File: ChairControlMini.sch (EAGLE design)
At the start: 36 parts, among them J1 Digital_0_7, J2 Analog, J3 Digital_8_13, J4 Analog, J5 Digital_0_7, SW1 SWITCH-DPDT3, X1 INPUT, X2 OUTPUT, X4 INPUT

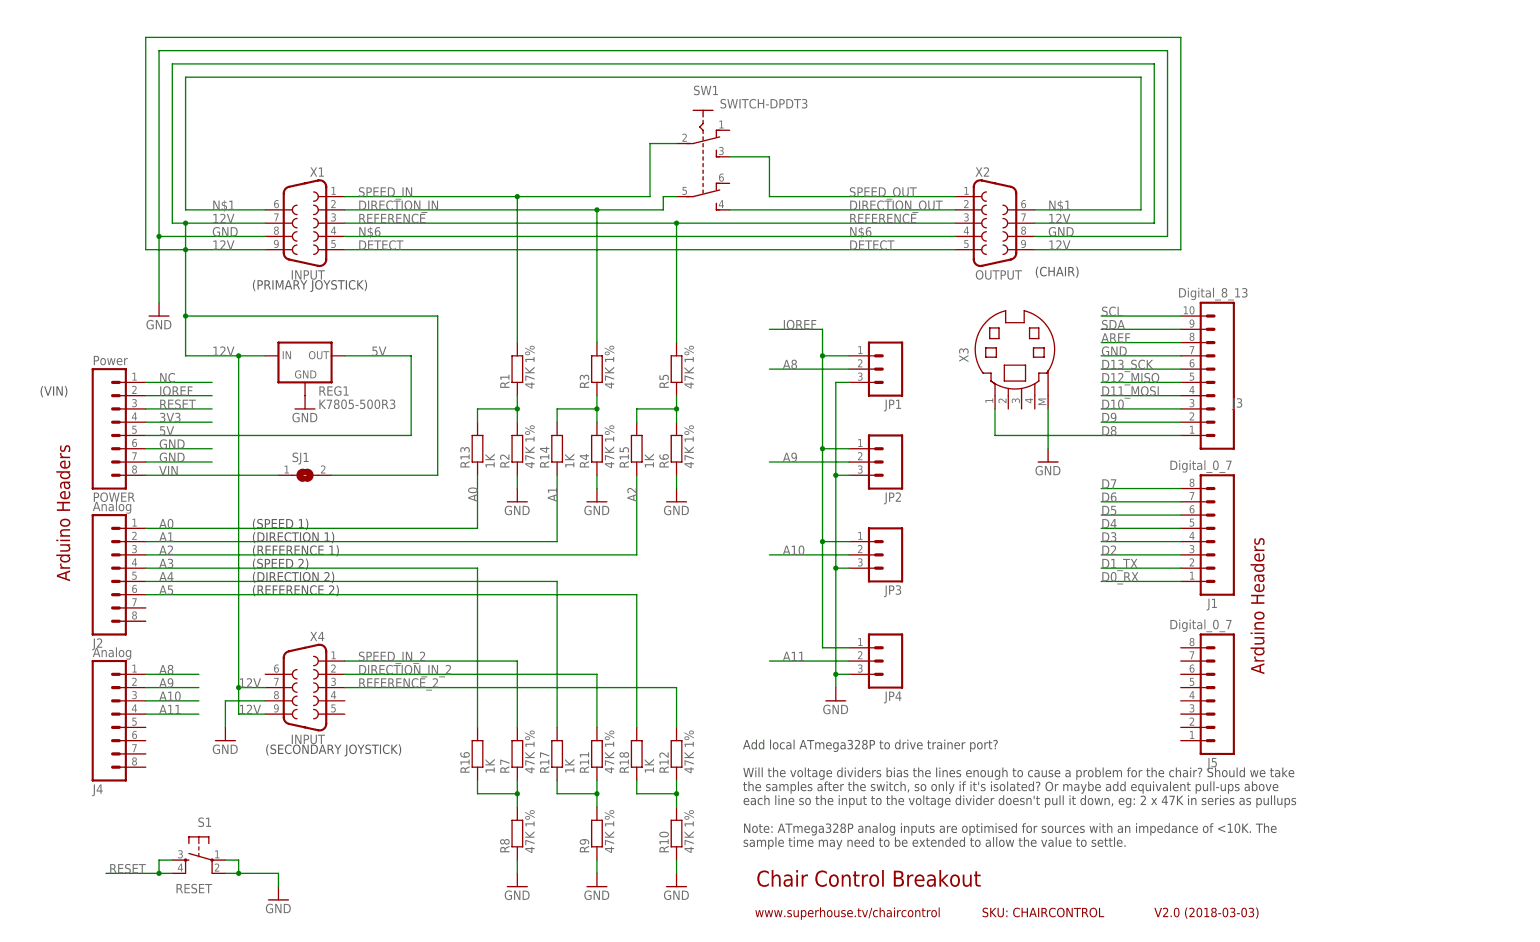
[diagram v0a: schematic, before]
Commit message: Added CAN interface and removed second joystick input
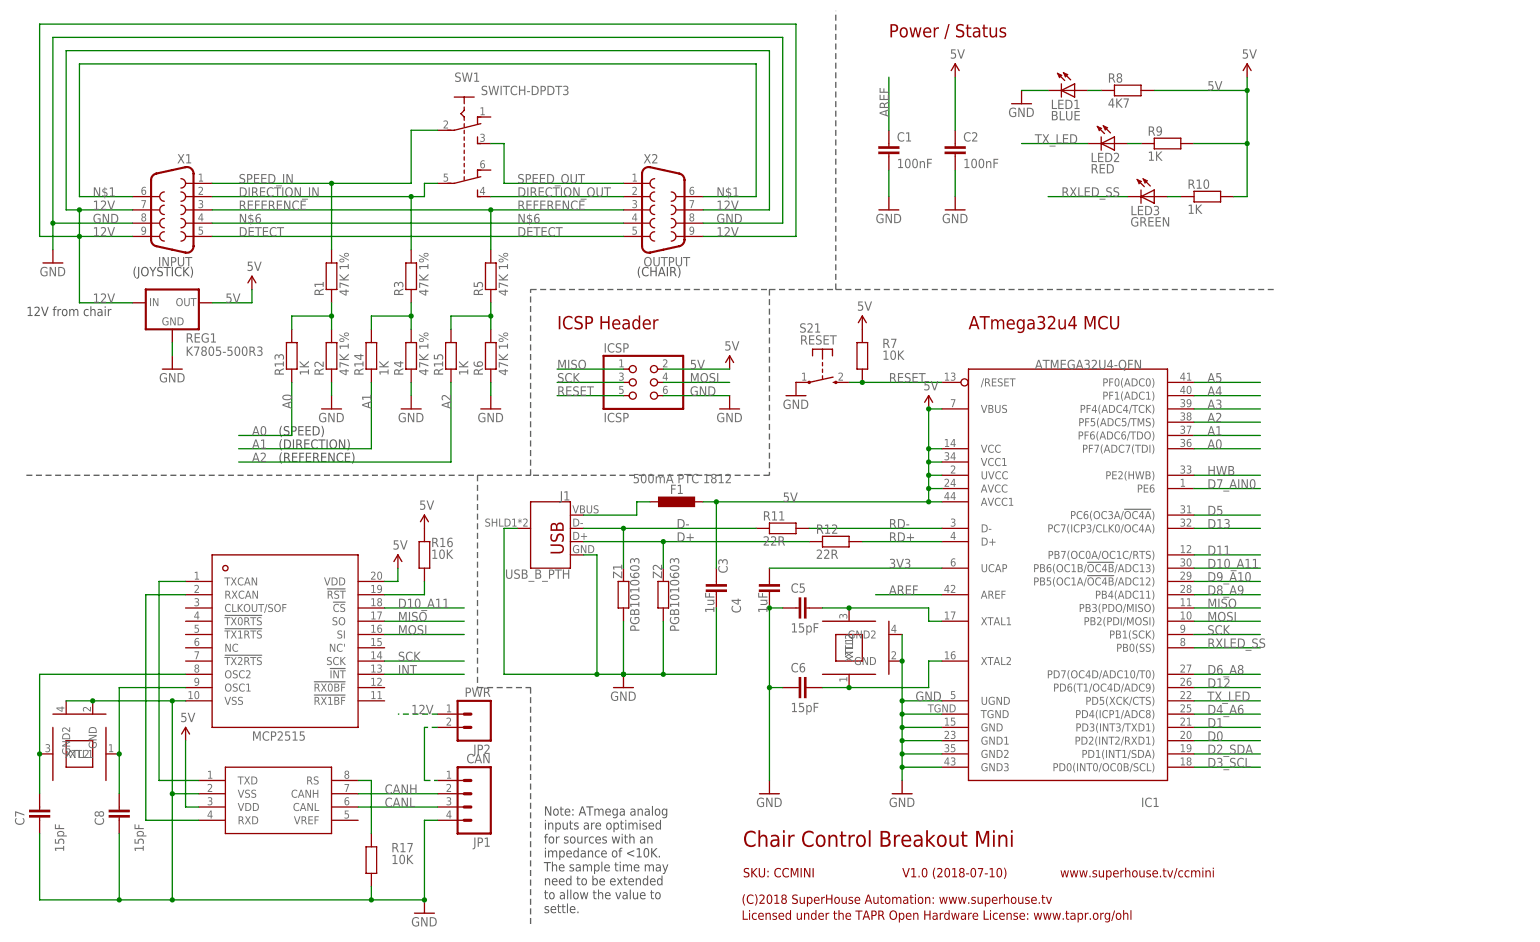
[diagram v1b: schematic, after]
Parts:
- removed J2, J4: Analog, freetronics-jon:M08PTH
- removed J3: Digital_8_13, freetronics-original:M100.1
- removed J5: Digital_0_7, freetronics:M08
- removed JP3, JP4: (no value), freetronics-jon:M03PTH
- removed POWER: Power, freetronics-original:M08
- removed R18: 1K, freetronics-jon:RESISTOR0603
- removed S1: RESET, freetronics:TAC_SWITCHPTH
- removed SJ1: (no value), freetronics-jon:SJN
- removed X3: (no value), freetronics-jon:MD04S
- removed X4: INPUT, SparkFun-Connectors:DB9MALE
- added C1, C2: 100nF, freetronics-master-v1.1:CAP0603
- added C3, C4: 1uF, freetronics-master-v1.1:CAP0603
- added C5, C6, C7, C8: 15pF, freetronics-master-v1.1:CAP0603
- added F1: 500mA PTC 1812, rcl:L-EUL1812
- added IC1: ATMEGA32U4-QFN, freetronics-jon:ATMEGA32U4-QFN
- added ICSP: ICSP, pinhead:PINHD-2X3
- added LED1: BLUE, freetronics-jon:LED0603
- added LED2: RED, freetronics-jon:LED0603
- added LED3: GREEN, freetronics-jon:LED0603
- added S21: RESET, freetronics-jon:TAC_SWITCH_2PINSMT
- added U$4: MCP2515, MCP2515:MCP2515
- added U1: MCP2551, freetronics-original:MCP2551
- added XTL1, XTL2: 16MHz, freetronics-jon:CRYSTAL-GND3X2
- added Z1, Z2: PGB1010603, freetronics-master-v1.1:RESISTOR0603
- J1: value Digital_0_7 -> USB_B_PTH; device freetronics:M08 -> SparkFun-Connectors:USB_B_PTH
- JP1: value (none) -> CAN; device freetronics-jon:M03PTH -> freetronics-jon:M04PTH
- JP2: value (none) -> PWR; device freetronics-jon:M03PTH -> freetronics-jon:M02PTH
- R10, R9: value 47K 1% -> 1K
- R11, R12: value 47K 1% -> 22R
- R16, R17: value 1K -> 10K; device freetronics-jon:RESISTOR0603 -> freetronics-master-v1.1:RESISTOR0603
- R7: value 47K 1% -> 10K; device freetronics-jon:RESISTOR0603 -> freetronics-master-v1.1:RESISTOR0603
- R8: value 47K 1% -> 4K7
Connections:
- removed net A10: J4.3, JP3.2
- removed net A11: J4.4, JP4.2
- removed net A8: J4.1, JP1.2
- removed net A9: J4.2, JP2.2
- removed net D0_RX: J1.1
- removed net D10: J3.3
- removed net D11_MOSI: J3.4
- removed net D12_MISO: J3.5
- removed net D13_SCK: J3.6
- removed net D1_TX: J1.2
- removed net D2: J1.3
- removed net D3: J1.4
- removed net D4: J1.5
- removed net D6: J1.7
- removed net D7: J1.8
- removed net D8: J3.1, X3.1
- removed net D9: J3.2
- removed net DIRECTION_IN_2: R11.2, X4.2
- removed net IOREF: JP1.1, JP2.1, JP3.1, JP4.1, POWER.2
- removed net NC: POWER.1
- removed net REFERENCE_2: R12.2, X4.3
- removed net SCL: J3.10
- removed net SDA: J3.9
- removed net SPEED_IN_2: R7.2, X4.1
- removed net VIN: POWER.8, SJ1.1
- new net CANH: JP1.2, U1.CANH
- new net CANL: JP1.3, U1.CANL
- new net D+: J1.D+, R12.1, Z2.2
- new net D-: J1.D-, R11.1, Z1.2
- new net D0: IC1.PD2(INT2/RXD1)
- new net D1: IC1.PD3(INT3/TXD1)
- new net D10_A11: IC1.PB6(OC1B/!OC4B!/ADC13), U$4.!CS
- new net D11: IC1.PB7(OC0A/OC1C/RTS)
- new net D12: IC1.PD6(T1/OC4D/ADC9)
- new net D13: IC1.PC7(ICP3/CLK0/OC4A)
- new net D2_SDA: IC1.PD1(INT1/SDA)
- new net D3_SCL: IC1.PD0(INT0/OC0B/SCL)
- new net D4_A6: IC1.PD4(ICP1/ADC8)
- new net D6_A8: IC1.PD7(OC4D/ADC10/T0)
- new net D7_AIN0: IC1.PE6
- new net D8_A9: IC1.PB4(ADC11)
- new net D9_A10: IC1.PB5(OC1A/!OC4B!/ADC12)
- new net HWB: IC1.PE2(HWB)
- new net INT: U$4.!INT
- new net MISO: IC1.PB3(PDO/MISO), ICSP.1, U$4.SO
- new net MOSI: IC1.PB2(PDI/MOSI), ICSP.4, U$4.SI
- new net N$10: R16.1, U$4.!RST
- new net N$11: C5.2, IC1.XTAL1, XTL1.XTL2
- new net N$12: C6.2, IC1.XTAL2, XTL1.XTL1
- new net N$13: U$4.RXCAN, U1.RXD
- new net N$14: C8.2, U$4.OSC1, XTL2.XTL1
- new net N$15: JP1.1, JP2.2
- new net N$16: R17.2, U1.RS
- new net N$18: C7.2, U$4.OSC2, XTL2.XTL2
- new net N$5: LED1.A, R8.1
- new net RD+: IC1.D+, R12.2
- new net RD-: IC1.D-, R11.2
- new net RXLED_SS: IC1.PB0(SS), LED3.C
- new net SCK: IC1.PB1(SCK), ICSP.3, U$4.SCK
- new net TX_LED: IC1.PD5(XCK/CTS), LED2.C
- new net USB+: F1.1, J1.VBUS
- net 12V: now also JP2.1; no longer SJ1.2, X4.7, X4.9
- net 3V3: now also C4.2, IC1.UCAP; no longer POWER.4
- net 5V: now also C2.1, C3.1, F1.2, IC1.AVCC, IC1.AVCC1, IC1.UVCC, IC1.VBUS, IC1.VCC, IC1.VCC1, ICSP.2, R10.2, R16.2, R7.2, R8.2, R9.2, U$4.VDD, U1.VDD; no longer POWER.5
- net A0: now also IC1.PF7(ADC7(TDI); no longer J2.1
- net A1: now also IC1.PF6(ADC6/TDO); no longer J2.2
- net A2: now also IC1.PF5(ADC5/TMS); no longer J2.3
- net A3: now also IC1.PF4(ADC4/TCK); no longer J2.4, R16.2
- net A4: now also IC1.PF1(ADC1); no longer J2.5, R17.2
- net A5: now also IC1.PF0(ADC0); no longer J2.6, R18.2
- net AREF: now also C1.1, IC1.AREF; no longer J3.8
- net D5: now also IC1.PC6(OC3A/!OC4A!); no longer J1.6
- net GND: now also C1.2, C2.2, C3.2, C4.1, C5.1, C6.1, C7.1, C8.1, IC1.GND, IC1.GND1, IC1.GND2, IC1.GND3, IC1.TGND, IC1.UGND, ICSP.6, J1.GND, J1.SHIELD, JP1.4, LED1.C, R17.1, S21.P, U$4.VSS, U1.VSS, XTL1.GND, XTL1.GND2, XTL2.GND, XTL2.GND2, Z1.1, Z2.1; no longer J3.7, JP1.3, JP2.3, JP3.3, JP4.3, POWER.6, POWER.7, R10.1, R8.1, R9.1, S1.1, S1.2, X3.5, X4.8
- net N$7: now also LED2.A, R9.1; no longer R16.1, R7.1, R8.2
- net N$8: now also LED3.A, R10.1; no longer R11.1, R17.1, R9.2
- net N$9: now also U$4.TXCAN, U1.TXD; no longer R10.2, R12.1, R18.1
- net RESET: now also IC1./RESET, ICSP.5, R7.1, S21.S; no longer POWER.3, S1.3, S1.4
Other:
- note added: "(C)2018 SuperHouse Automation: www.superhouse.tv"
- note added: "(DIRECTION)"
- note added: "(JOYSTICK)"
- note added: "(REFERENCE)"
- note added: "(SPEED)"
- note added: "12V from chair"
- note added: "ATmega32u4 MCU"
- note added: "Chair Control Breakout Mini"
- note added: "ICSP Header"
- note added: "Licensed under the TAPR Open Hardware License: www.tapr.org/ohl"
- note added: "Note: ATmega analog inputs are optimised for sources with an impedance of <10K. The sample time may need to be extended to allow the value to settle."
- note added: "Power / Status"
- note added: "SKU: CCMINI"
- note added: "V1.0 (2018-07-10)"
- note added: "www.superhouse.tv/ccmini"
- note removed: "(DIRECTION 1)"
- note removed: "(DIRECTION 2)"
- note removed: "(PRIMARY JOYSTICK)"
- note removed: "(REFERENCE 1)"
- note removed: "(REFERENCE 2)"
- note removed: "(SECONDARY JOYSTICK)"
- note removed: "(SPEED 1)"
- note removed: "(SPEED 2)"
- note removed: "(VIN)"
- note removed: "Add local ATmega328P to drive trainer port? Will the voltage dividers bias the lines enough to cause a problem for the chair? Should we take the samples after the switch, so only if it's isolated? Or maybe add equivalent pull-ups above each line so the input to the voltage divider doesn't pull it down, eg: 2 x 47K in series as pullups Note: ATmega328P analog inputs are optimised for sources with 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"
- note removed: "Arduino Headers"
- note removed: "Chair Control Breakout"
- note removed: "SKU: CHAIRCONTROL"
- note removed: "V2.0 (2018-03-03)"
- note removed: "www.superhouse.tv/chaircontrol"
- moved on the sheet: R1, R10, R11, R12, R13, R14, R15, R16, R17, R2, R3, R4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

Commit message: Added power source selection and DRC for v1.0 release
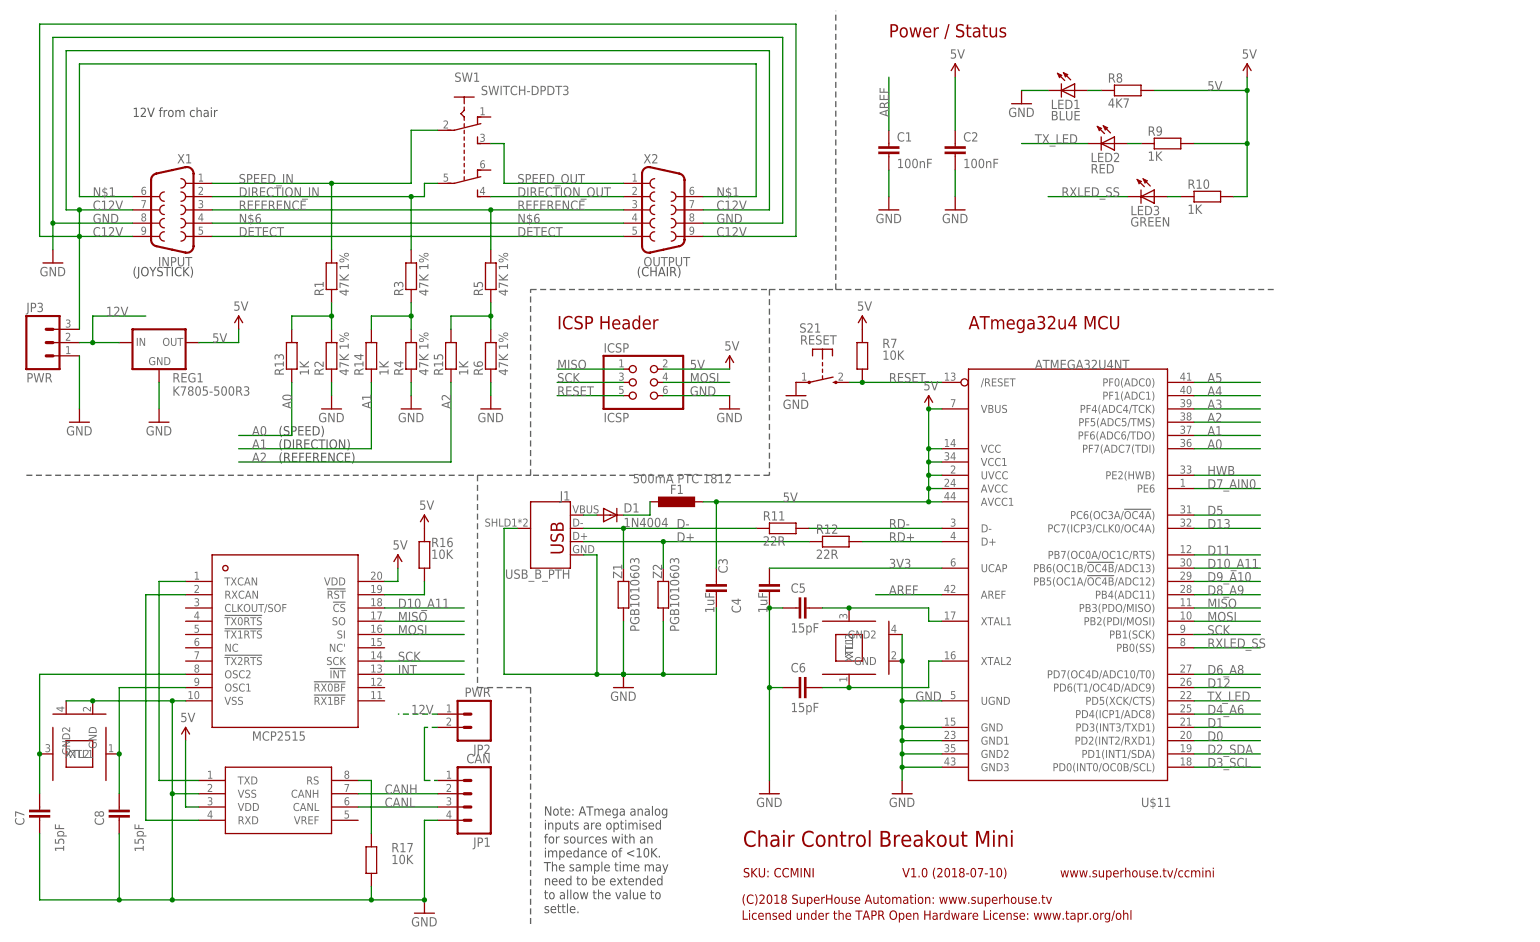
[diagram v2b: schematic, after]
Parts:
- removed IC1: ATMEGA32U4-QFN, freetronics-jon:ATMEGA32U4-QFN
- added D1: 1N4004, freetronics-jon:DIODESMB
- added JP3: PWR, freetronics-jon:M03PTH
- added U$11: ATMEGA32U4NT, freetronics-jon:ATMEGA32U4NT
- XTL2: value 16MHz -> 8MHz
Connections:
- new net C12V: JP3.3, X1.7, X1.9, X2.7, X2.9
- new net N$17: D1.C, F1.1
- net 12V: now also JP3.2; no longer X1.7, X1.9, X2.7, X2.9
- net 3V3: now also U$11.UCAP; no longer IC1.UCAP
- net 5V: now also U$11.AVCC, U$11.AVCC1, U$11.UVCC, U$11.VBUS, U$11.VCC, U$11.VCC1; no longer IC1.AVCC, IC1.AVCC1, IC1.UVCC, IC1.VBUS, IC1.VCC, IC1.VCC1
- net A0: now also U$11.PF7(ADC7(TDI); no longer IC1.PF7(ADC7(TDI)
- net A1: now also U$11.PF6(ADC6/TDO); no longer IC1.PF6(ADC6/TDO)
- net A2: now also U$11.PF5(ADC5/TMS); no longer IC1.PF5(ADC5/TMS)
- net A3: now also U$11.PF4(ADC4/TCK); no longer IC1.PF4(ADC4/TCK)
- net A4: now also U$11.PF1(ADC1); no longer IC1.PF1(ADC1)
- net A5: now also U$11.PF0(ADC0); no longer IC1.PF0(ADC0)
- net AREF: now also U$11.AREF; no longer IC1.AREF
- net D0: now also U$11.PD2(INT2/RXD1); no longer IC1.PD2(INT2/RXD1)
- net D1: now also U$11.PD3(INT3/TXD1); no longer IC1.PD3(INT3/TXD1)
- net D10_A11: now also U$11.PB6(OC1B/!OC4B!/ADC13); no longer IC1.PB6(OC1B/!OC4B!/ADC13)
- net D11: now also U$11.PB7(OC0A/OC1C/RTS); no longer IC1.PB7(OC0A/OC1C/RTS)
- net D12: now also U$11.PD6(T1/OC4D/ADC9); no longer IC1.PD6(T1/OC4D/ADC9)
- net D13: now also U$11.PC7(ICP3/CLK0/OC4A); no longer IC1.PC7(ICP3/CLK0/OC4A)
- net D2_SDA: now also U$11.PD1(INT1/SDA); no longer IC1.PD1(INT1/SDA)
- net D3_SCL: now also U$11.PD0(INT0/OC0B/SCL); no longer IC1.PD0(INT0/OC0B/SCL)
- net D4_A6: now also U$11.PD4(ICP1/ADC8); no longer IC1.PD4(ICP1/ADC8)
- net D5: now also U$11.PC6(OC3A/!OC4A!); no longer IC1.PC6(OC3A/!OC4A!)
- net D6_A8: now also U$11.PD7(OC4D/ADC10/T0); no longer IC1.PD7(OC4D/ADC10/T0)
- net D7_AIN0: now also U$11.PE6; no longer IC1.PE6
- net D8_A9: now also U$11.PB4(ADC11); no longer IC1.PB4(ADC11)
- net D9_A10: now also U$11.PB5(OC1A/!OC4B!/ADC12); no longer IC1.PB5(OC1A/!OC4B!/ADC12)
- net GND: now also JP3.1, U$11.GND, U$11.GND1, U$11.GND2, U$11.GND3, U$11.UGND; no longer IC1.GND, IC1.GND1, IC1.GND2, IC1.GND3, IC1.TGND, IC1.UGND
- net HWB: now also U$11.PE2(HWB); no longer IC1.PE2(HWB)
- net MISO: now also U$11.PB3(PDO/MISO); no longer IC1.PB3(PDO/MISO)
- net MOSI: now also U$11.PB2(PDI/MOSI); no longer IC1.PB2(PDI/MOSI)
- net N$11: now also U$11.XTAL1; no longer IC1.XTAL1
- net N$12: now also U$11.XTAL2; no longer IC1.XTAL2
- net RD+: now also U$11.D+; no longer IC1.D+
- net RD-: now also U$11.D-; no longer IC1.D-
- net RESET: now also U$11./RESET; no longer IC1./RESET
- net RXLED_SS: now also U$11.PB0(SS); no longer IC1.PB0(SS)
- net SCK: now also U$11.PB1(SCK); no longer IC1.PB1(SCK)
- net TX_LED: now also U$11.PD5(XCK/CTS); no longer IC1.PD5(XCK/CTS)
- net USB+: now also D1.A; no longer F1.1
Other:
- moved on the sheet: REG1
